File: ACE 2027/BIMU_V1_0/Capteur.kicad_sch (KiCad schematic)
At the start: 5 parts, among them J301 Thermal_ResistanceM, U301 LSM6DS3

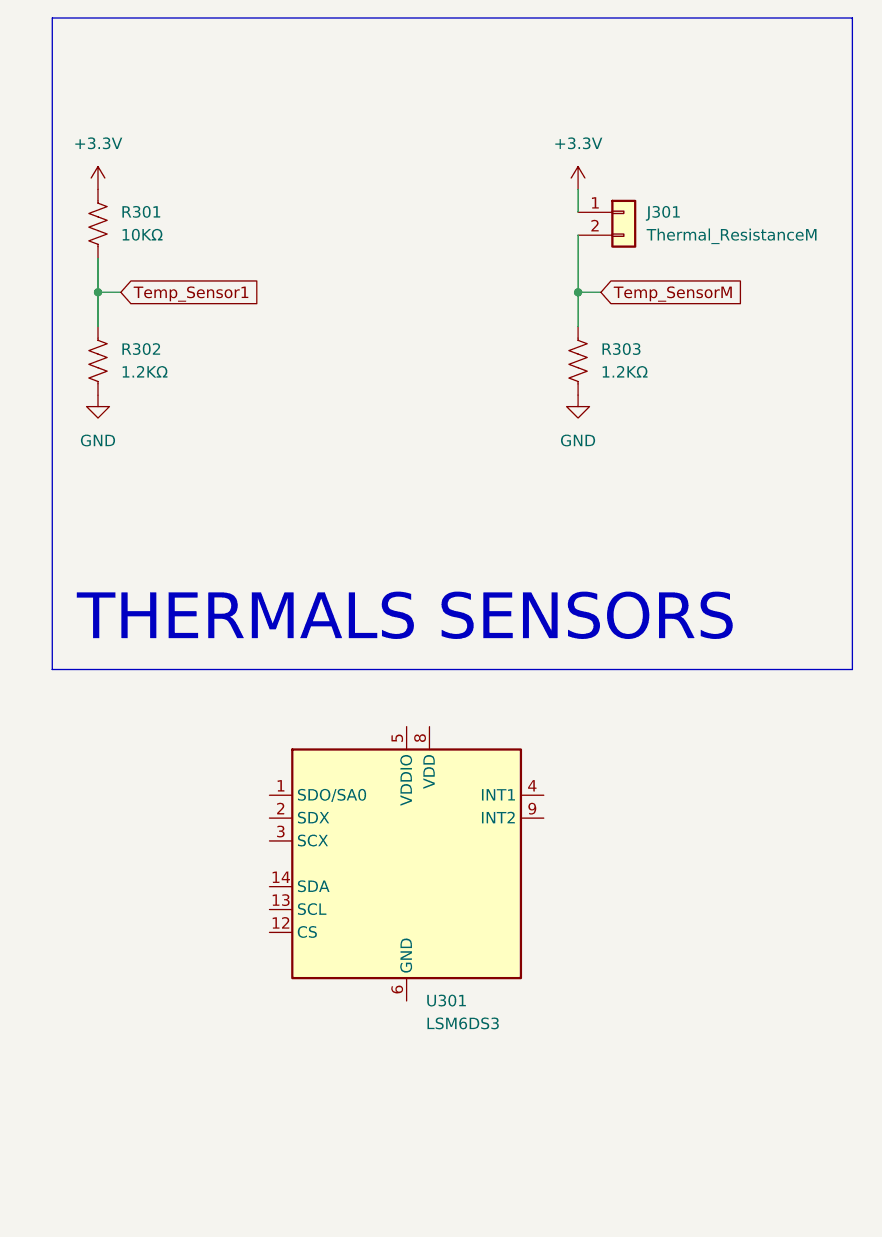
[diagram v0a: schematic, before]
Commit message: Avancement of different part of the schematic
Add and reorganize numerous symbol definitions and annotations in Alimentation.kicad_sch: new TestPoint, LED, R_US/Resistor symbols, BAV99 diode, MountingHole, AP7361C-33E regulator, power/GND symbol instances, and associated symbol variants. Add global CAN_P/CAN_N labels, layout rectangles and text (ESD protection, current rating), and adjust wires/junction coordinates. Also update BIMU_V_1.kicad_pcb, BIMU_V_1.kicad_sch, Capteur.kicad_sch, Controle.kicad_sch and fp-info-cache; add several backup .zip files and a Controle.kicad_sch-bak file.
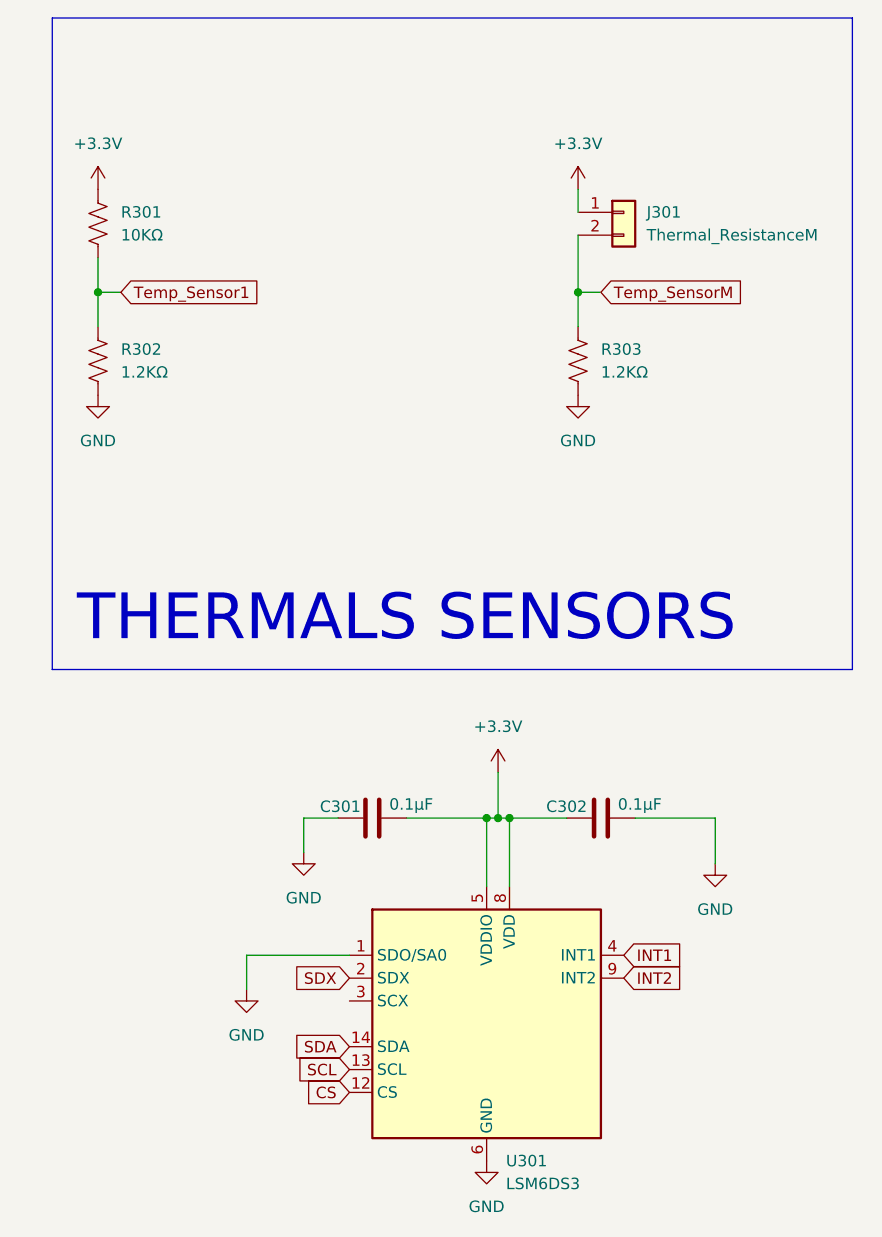
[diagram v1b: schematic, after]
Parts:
- added C301, C302: 0.1μF, Capacitor_SMD:C_0603_1608Metric_Pad1.08x0.95mm_HandSolder, symbol Device:C
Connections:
- net +3.3V: now also U301.5 (VDDIO), U301.8 (VDD), C301.1, C302.2
- net GND: now also U301.1 (SDO/SA0), U301.6 (GND), U301.7 (GND), C301.2, C302.1
- net CS: now reaches U301.12 (CS)
- net SCL: now reaches U301.13 (SCL)
- net SDA: now reaches U301.14 (SDA)
- net SDX: now reaches U301.2 (SDX)
- net INT1: now reaches U301.4 (INT1)
- net INT2: now reaches U301.9 (INT2)
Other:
- moved on the sheet: U301
